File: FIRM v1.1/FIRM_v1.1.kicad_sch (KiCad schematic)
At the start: 116 parts, among them J2 Conn_01x02_Pin, Q1 IRLML6402, U1 W25N04KVZEIR, U10 STM32F446ZCHx, U2 STM32H743VIHx, U3 ADXL371, U5 INA219AxDCN, U6 MIC5219-3.3YM5, U9 A-USBC-20F0-EA-GSR05, Y1 25 MHz, Y2 12 MHz

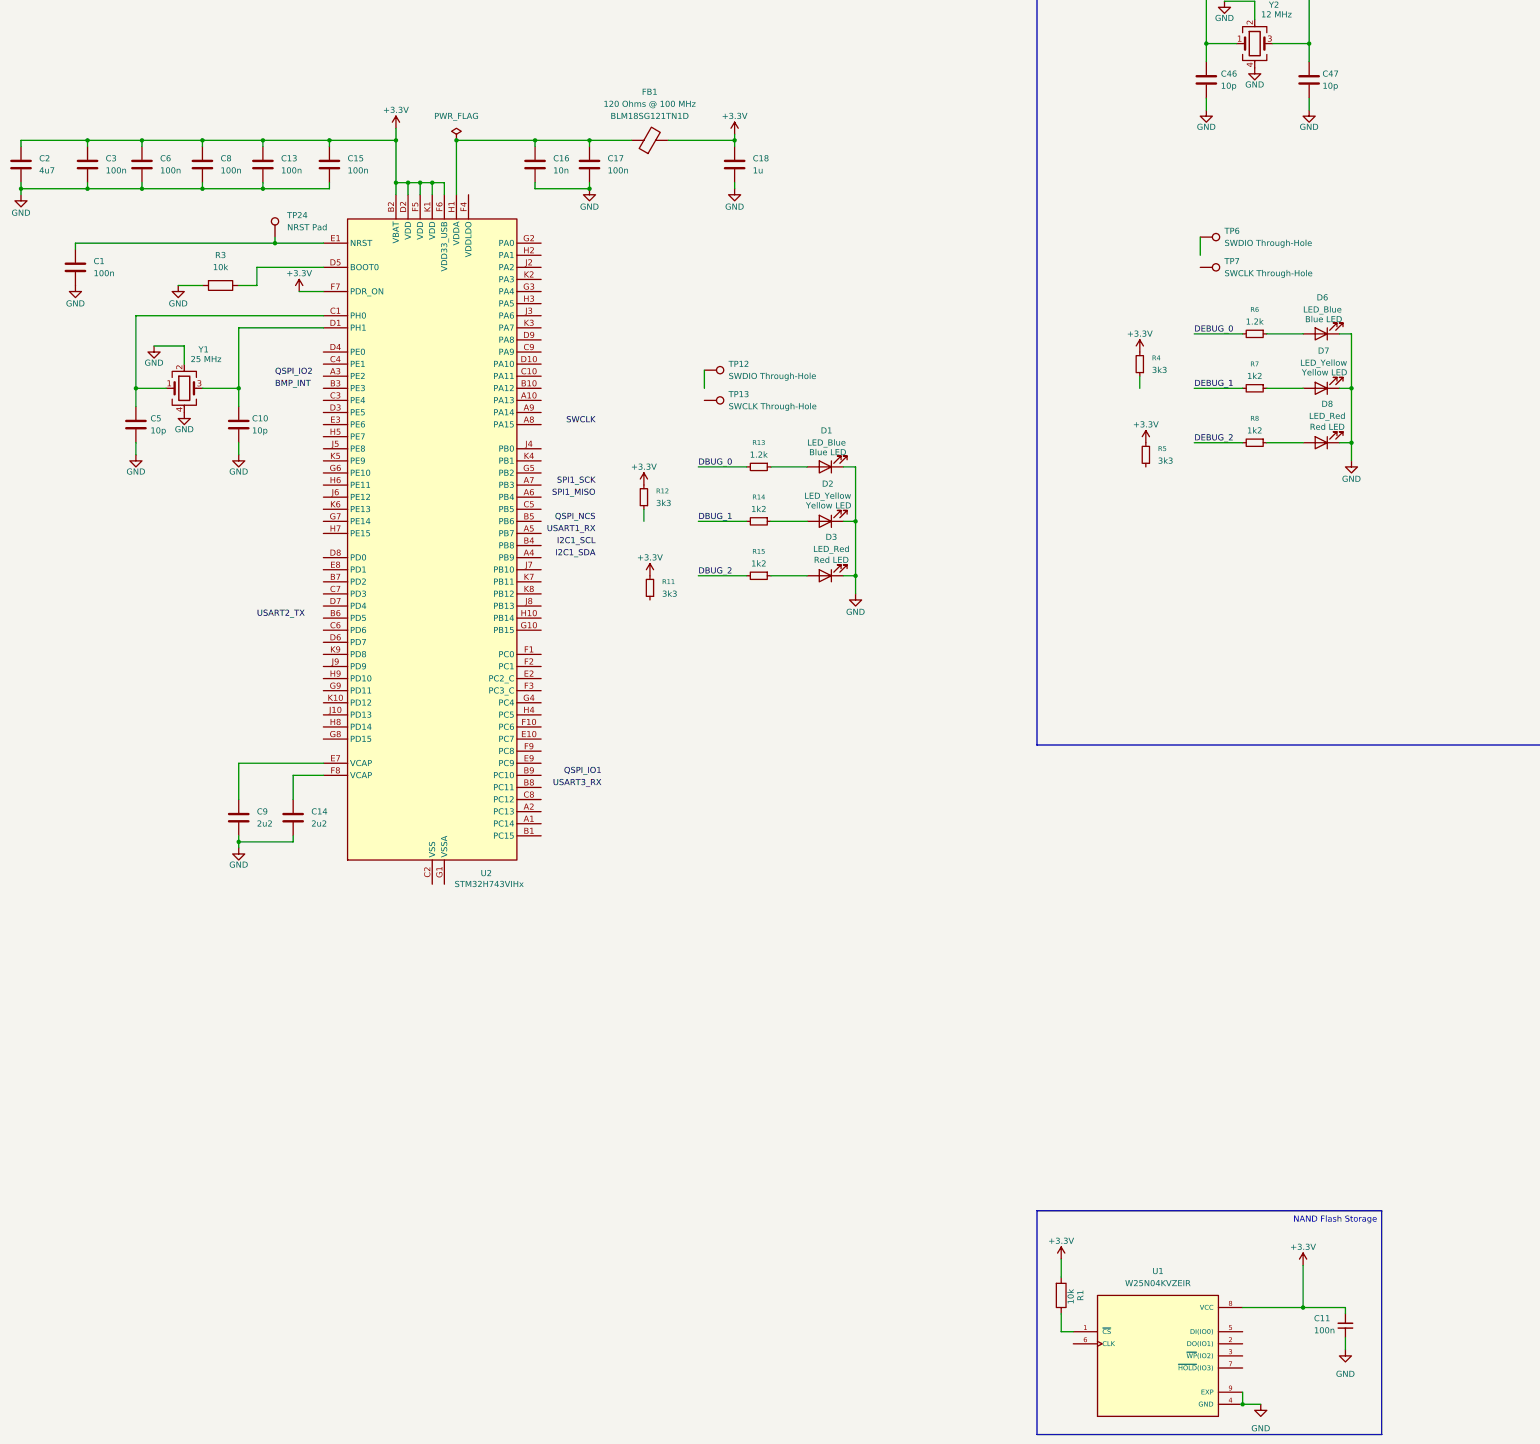
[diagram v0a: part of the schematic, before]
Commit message: Added new flash chip
Set up quadSPI with the new 1gbit flash chip.
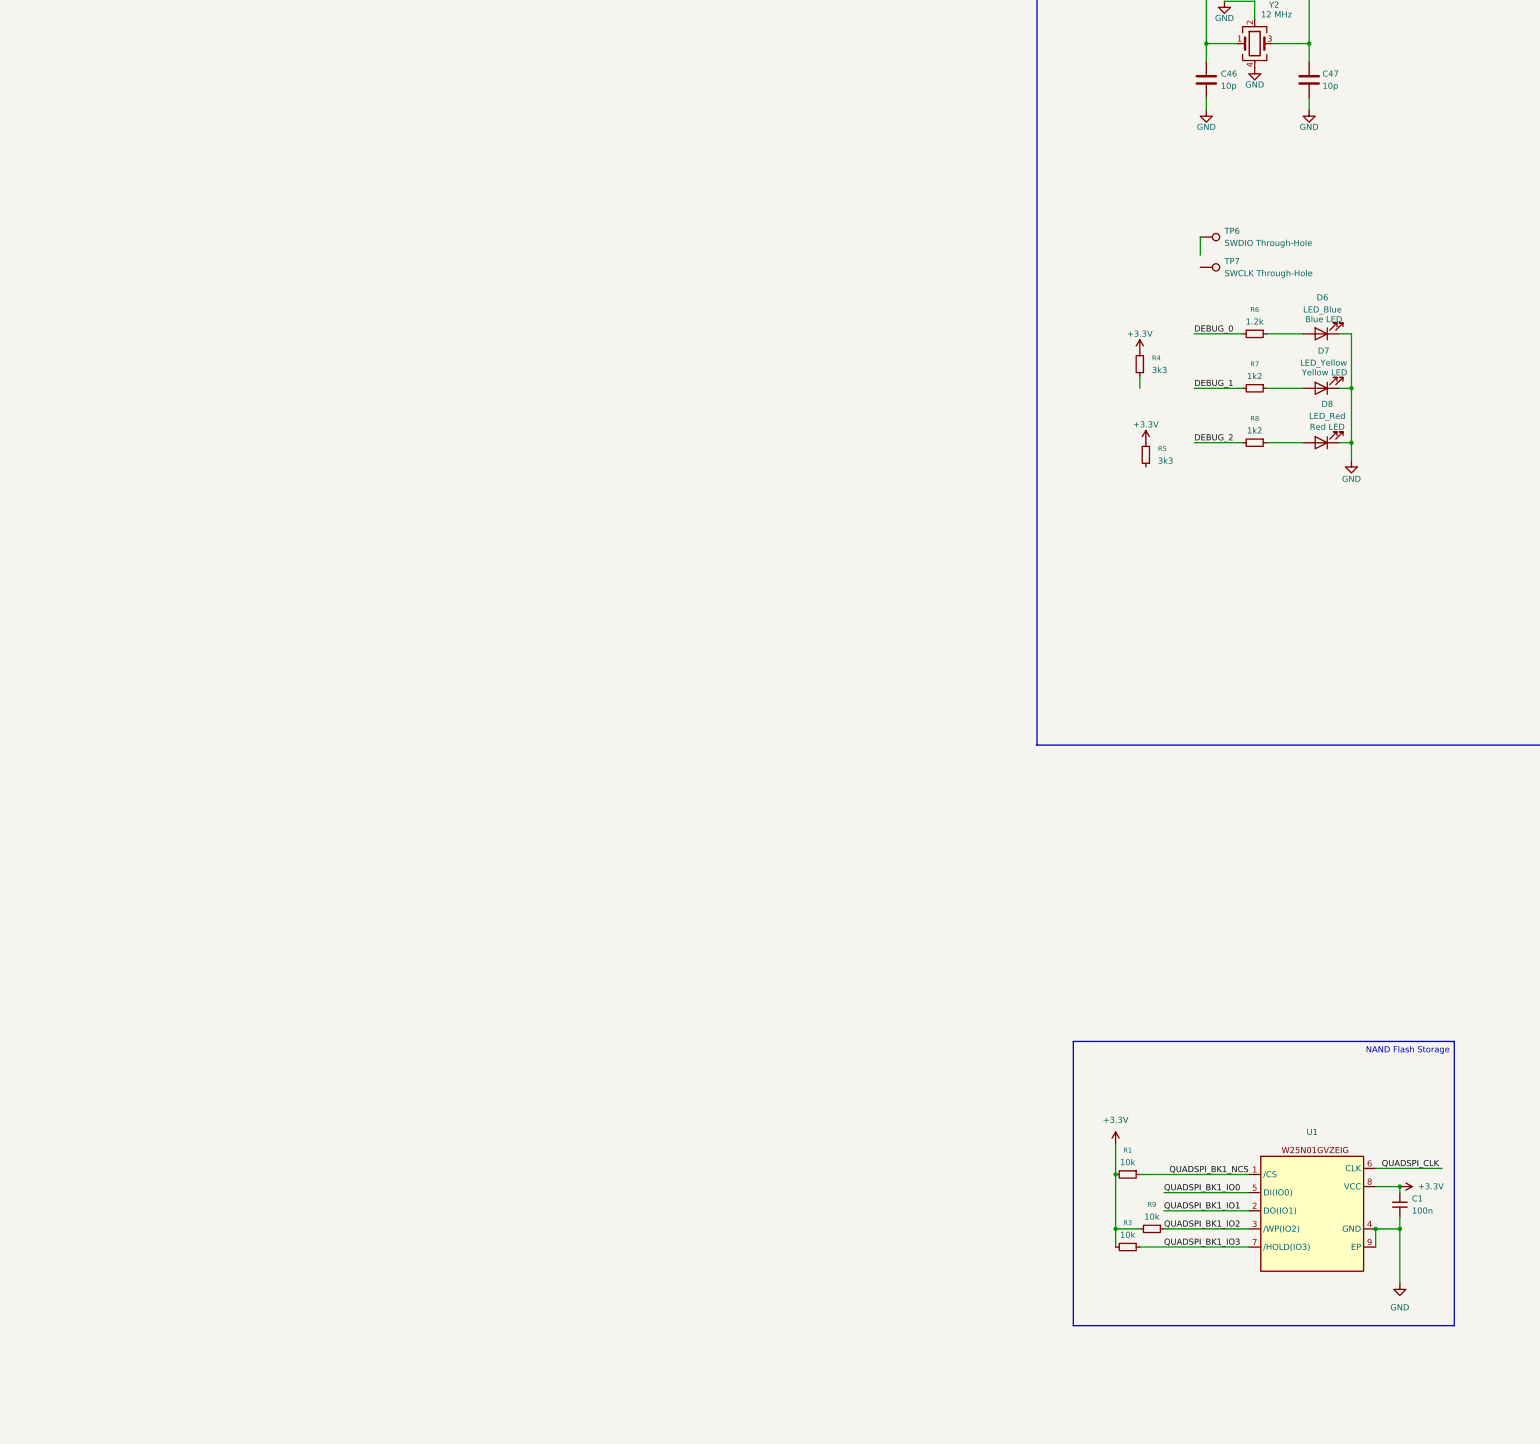
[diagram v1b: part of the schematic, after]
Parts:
- removed C1, C13, C15, C17, C3, C6, C8: 100n, Capacitor_SMD:C_0402_1005Metric, symbol Device:C
- removed C10, C5: 10p, Capacitor_SMD:C_0402_1005Metric, symbol Device:C
- removed C11: 100n, Capacitor_SMD:C_0402_1005Metric, symbol Device:C_Small
- removed C14, C9: 2u2, Capacitor_SMD:C_0402_1005Metric, symbol Device:C
- removed C16: 10n, Capacitor_SMD:C_0402_1005Metric, symbol Device:C
- removed C18: 1u, Capacitor_SMD:C_0402_1005Metric, symbol Device:C
- removed C2: 4u7, Capacitor_SMD:C_0402_1005Metric, symbol Device:C
- removed D1: LED_Blue, LED_SMD:LED_0402_1005Metric, symbol Device:LED
- removed D2: LED_Yellow, LED_SMD:LED_0402_1005Metric, symbol Device:LED
- removed D3: LED_Red, LED_SMD:LED_0402_1005Metric, symbol Device:LED
- removed FB1: 120 Ohms @ 100 MHz, Inductor_SMD:L_0603_1608Metric, symbol Device:FerriteBead
- removed R1, R3: 10k, Resistor_SMD:R_0402_1005Metric, symbol Device:R
- removed R11, R12: 3k3, Resistor_SMD:R_0402_1005Metric, symbol Device:R_Small
- removed R13: 1.2k, Resistor_SMD:R_0402_1005Metric, symbol Device:R_Small
- removed R14, R15: 1k2, Resistor_SMD:R_0402_1005Metric, symbol Device:R_Small
- removed TP12: SWDIO Through-Hole, connectors:Testpoint_1.5x1.5mm_1.0mm, symbol Connector:TestPoint
- removed TP13: SWCLK Through-Hole, connectors:Testpoint_1.5x1.5mm_1.0mm, symbol Connector:TestPoint
- removed TP24: NRST Pad, connectors:smd_test_pads_1mm, symbol Connector:TestPoint
- removed U1: W25N04KVZEIR, IC_W25N04KVZEIR:IC_W25N04KVZEIR, symbol W25N04KVZEIR:W25N04KVZEIR
- removed U2: STM32H743VIHx, Package_BGA:TFBGA-100_8x8mm_Layout10x10_P0.8mm, symbol MCU_ST_STM32H7:STM32H743VIHx
- removed Y1: 25 MHz, Crystal:Crystal_SMD_3225-4Pin_3.2x2.5mm, symbol Device:Crystal_GND24
- added C1: 100n, Package_SO:SOIC-8_3.9x4.9mm_P1.27mm, symbol Device:C_Small
- added R1, R3, R9: 10k, symbol Device:R_Small
- added U1: (no value), Custom:W25N01GVZEIG, symbol Custom:W25N01GVZEIG
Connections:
- net +3.3V: now also C1.1, R1.2, R3.2, R9.2, U1.8 (VCC)
- net GND: now also C1.2, U1.4 (GND), U1.9 (EP)
- net QUADSPI_CLK: now also U1.6 (CLK)
- new net: U3.10 (RES), U3.13 (GND), U3.16 (GND)
- new net QUADSPI_BK1_IO0: U1.5 (DI(IO0))
- new net QUADSPI_BK1_IO1: U1.2 (DO(IO1))
- new net QUADSPI_BK1_IO2: R9.1, U1.3 (/WP(IO2))
- new net QUADSPI_BK1_IO3: R3.1, U1.7 (/HOLD(IO3))
- new net QUADSPI_BK1_NCS: R1.1, U1.1 (/CS)
